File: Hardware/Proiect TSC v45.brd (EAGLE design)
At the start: 170.2 x 111.3 mm, 103 parts, among them IC1 XC6220A331MR-G, IC2 BD5229G-TR, J1 SAMACSYS_PARTS_USB4110-GF-A, J2 112A-TAAR-R03_ATTEND, J3 FH34SRJ-24S-0.5SH_99_, J4 QWIIC_RIGHT_ANGLE, Q1 20V/4.2A/52mΩ/1.4W, Q2 SI1308EDL-T1-GE3, Q3 20V/4.2A/52mΩ/1.4W, U1 ESP32-C6-WROOM-1-N8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

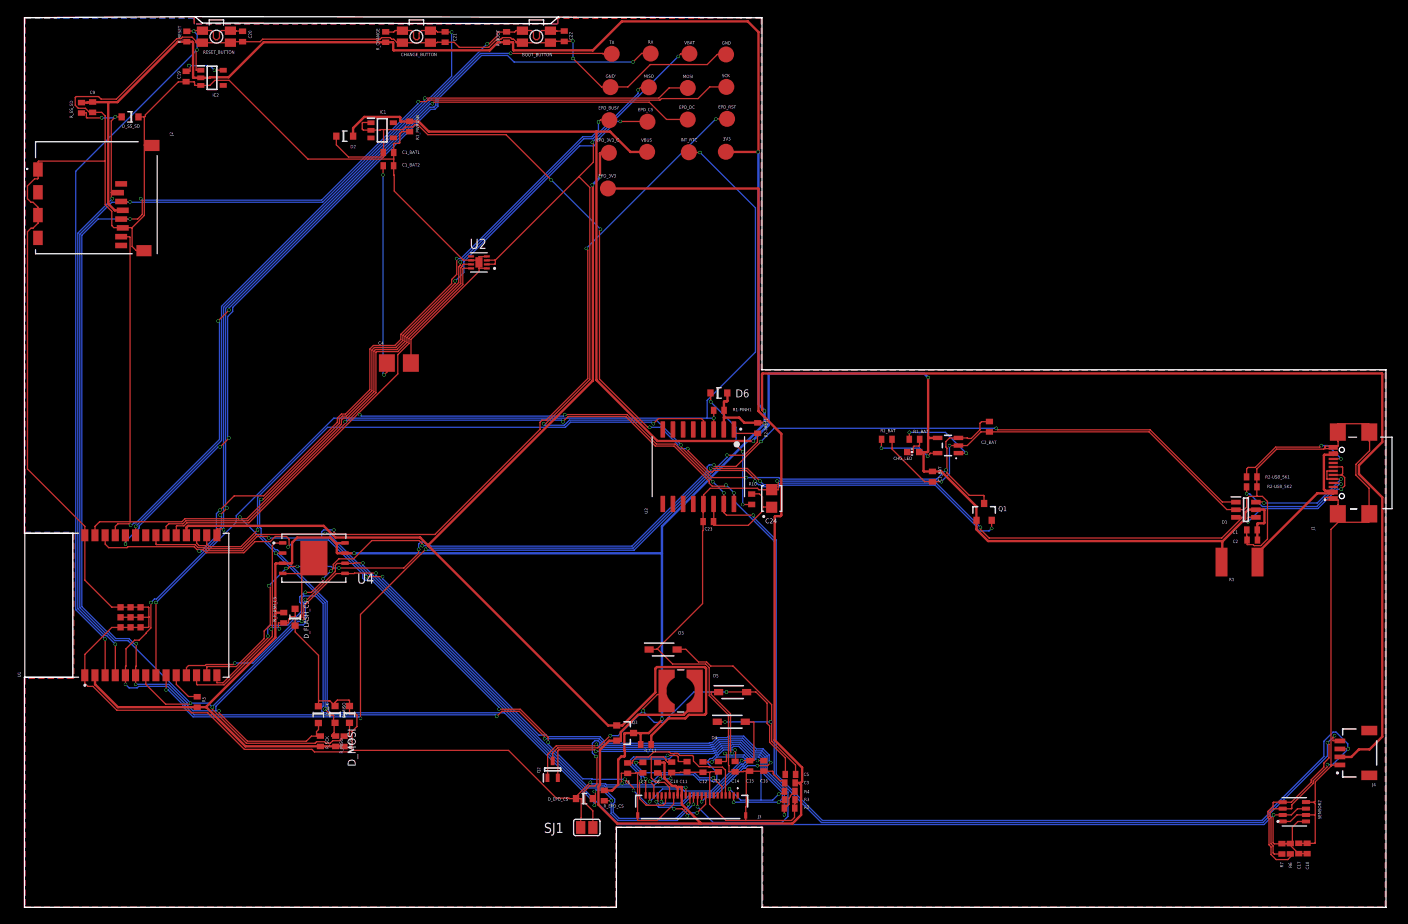
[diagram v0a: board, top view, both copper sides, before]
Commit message: Solved wrong routes, added ground plane, fixed silkscreen
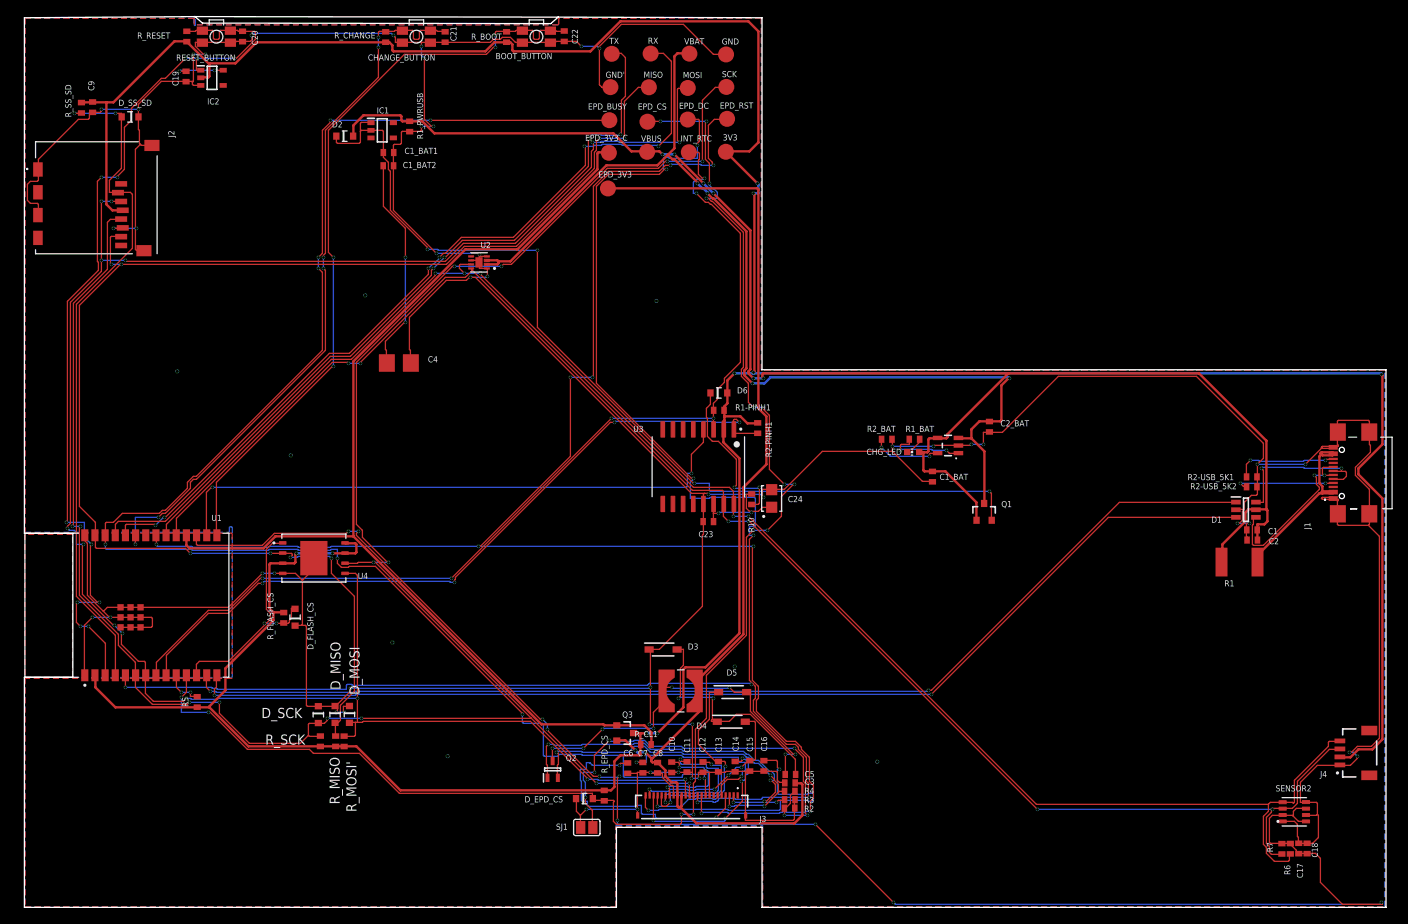
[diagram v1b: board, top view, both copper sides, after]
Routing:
- net SDA: track 246.2 -> 203.1 mm, vias 7 -> 6
- net SCL: track 251.6 -> 209.5 mm, vias 6 -> 5
- net GND: track 735.5 -> 695.5 mm, vias 9 -> 53
- net I2C_PW: track 169.7 -> 205.1 mm, vias 2 -> 10
- net EPD_3V3: track 163.5 -> 133.2 mm, vias 0 -> 2
- net EPD_BUSY: track 177.8 -> 200.0 mm, vias 12 -> 8
- net EPD_RST: track 187.6 -> 206.6 mm
- net EPD_3V3_C: track 155.1 -> 137.7 mm, vias 2 -> 0
- net EPD_DC: track 230.6 -> 213.8 mm
- net RESET: track 100.5 -> 116.5 mm, vias 3 -> 11
- net N$7: track 17.4 -> 33.2 mm, vias 0 -> 2
- net VBAT: track 145.4 -> 132.2 mm, vias 6 -> 4
- net EPD_CS: track 199.8 -> 187.1 mm, vias 8 -> 14
- net N$19: track 22.9 -> 35.6 mm
- net 32KHZ: track 104.1 -> 92.4 mm
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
